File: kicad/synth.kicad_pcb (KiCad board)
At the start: 2 copper layers, 154.9 x 102.9 mm, 279 parts, among them CON101 SD_Card, CON201 K375A (DJK-02A), J301 KATE_3.5MM_6, J302 KATE_3.5MM_6, J401 KATE_3.5MM_6, J402 KATE_3.5MM_6, J403 KATE_3.5MM_6, P101 CONN_01X05, P102 CONN_01X03, P103 CONN_01X03, P104 47346-0001, P105 CONN_01X01, P106 DIN_5, P301 CONN_02X04, P302 CONN_01X03, Q101 MMBTA42, Q201 FDS6675, Q202 IRF7313PBF, Q301 Si2301DS, Q302 BC817, Q401 Si2301DS, Q402 Si2301DS, Q403 Si2301DS, SW101 SW_PUSH, SW102 SW_PUSH, T201 TRANS_CUSTOM, U101 STM32F405R, U102 USBLC6-2, U103 AD1955, U104 HCPL0453, U201 LM78L12ACZ, U202 79L12, U203 MC33269-SO8, U204 TPS76333DBV, U205 LP2985LV, U206 LP2985LV, U301 OP275S, U302 OP275S, U303 LM4864, U304 LM4864, U305 OP275S, U401 AD824, Y101 25MHz

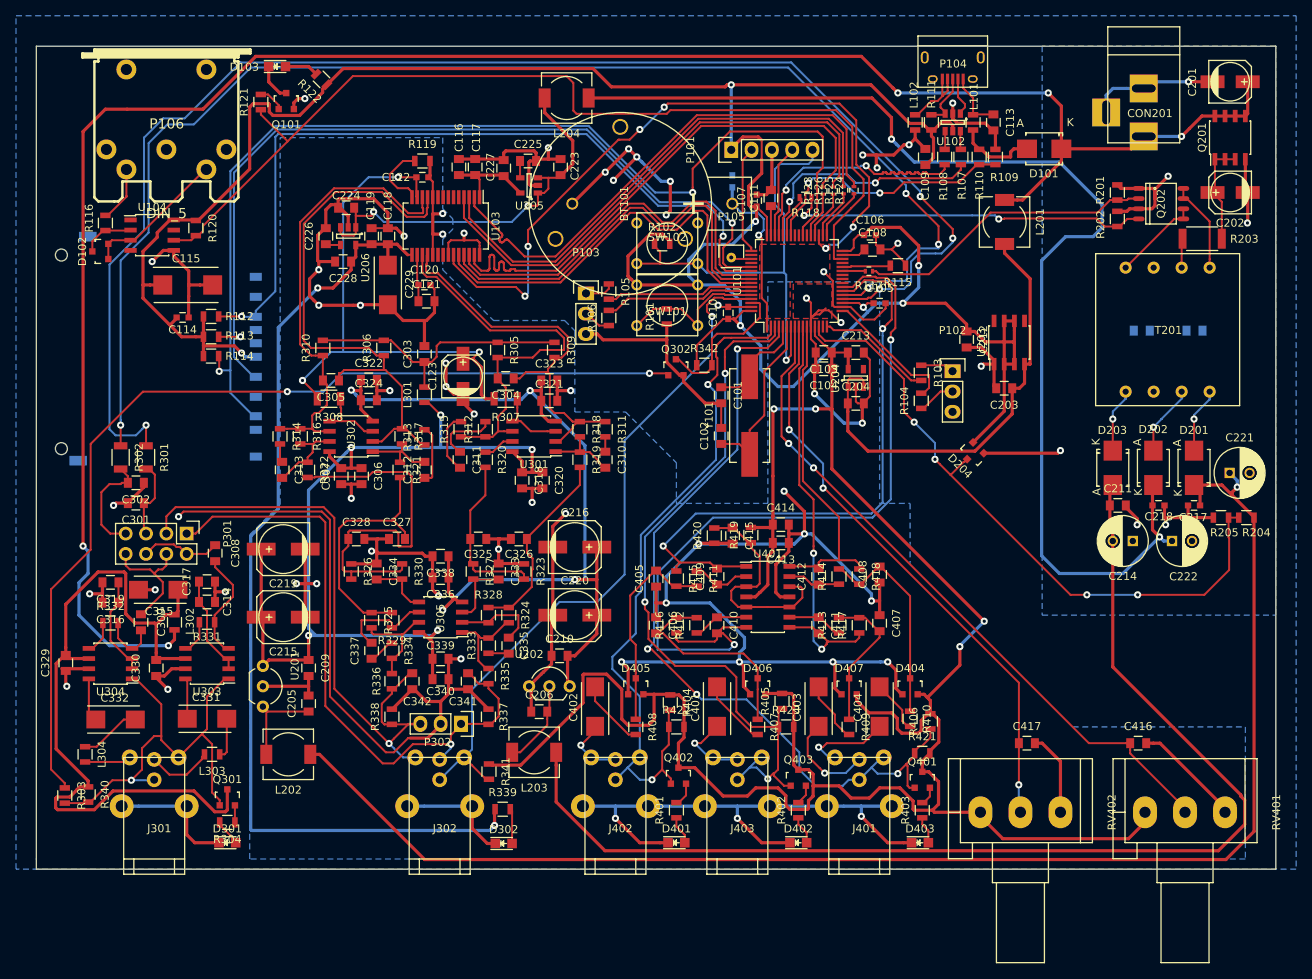
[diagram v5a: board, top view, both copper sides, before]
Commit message: version sent to rezonit
modified usb connector pads to smd
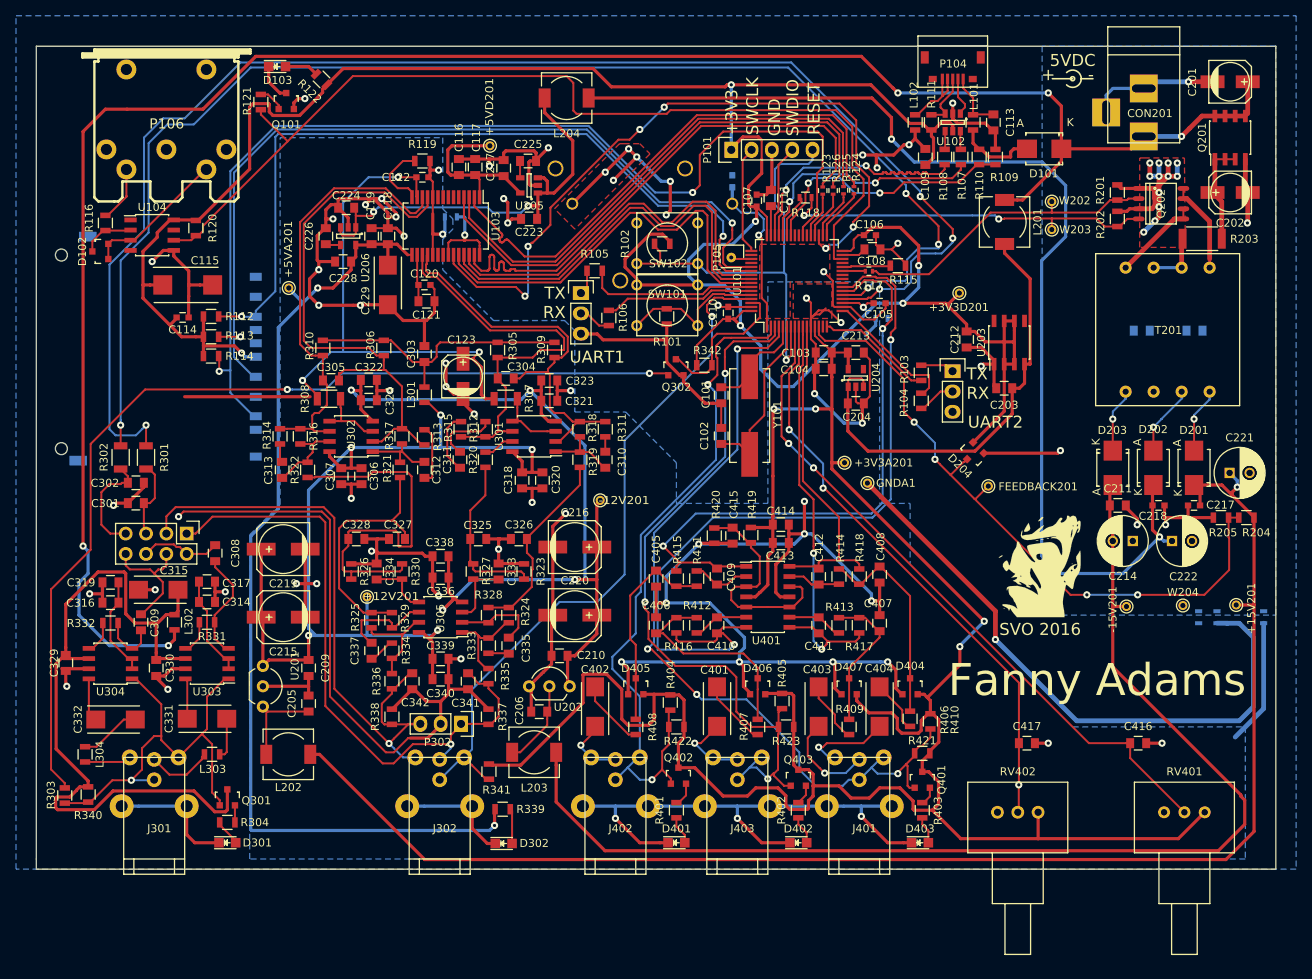
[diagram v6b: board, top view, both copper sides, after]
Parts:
- added +12V201: TST, Connect:PINTST, F.Cu at (54.0, 119.6)
- added +15V201: TST+15V, Connect:PINTST, F.Cu at (162.7, 120.7)
- added +3V3A201: TST, Connect:PINTST, F.Cu at (113.7, 102.9)
- added +3V3D201: TST, Connect:PINTST, F.Cu at (128.1, 81.7)
- added +5VA201: TST, Connect:PINTST, F.Cu at (44.3, 81.0)
- added +5VD201: TST, Connect:PINTST, F.Cu at (69.4, 63.2)
- added -12V201: TST, Connect:PINTST, F.Cu at (83.2, 107.6)
- added -15V201: TST-15V, Connect:PINTST, F.Cu at (149.0, 120.8)
- added FEEDBACK201: TST, Connect:PINTST, F.Cu at (131.7, 105.8)
- added G***: LOGO, svo_xface:svo-xface, F.Cu at (136.9, 115.8)
- added GNDA1: TST, Connect:PINTST, F.Cu at (116.6, 105.4)
- added JP101: Jumper_NC_Small, Resistors_SMD:R_0603, B.Cu at (64.5, 72.1)
- added JP102: Jumper_NC_Small, Resistors_SMD:R_0603, B.Cu at (118.4, 84.8)
- added JP103: Jumper_NC_Small, Resistors_SMD:R_0603, B.Cu at (158.0, 122.2)
- added JP104: Jumper_NC_Small, Resistors_SMD:R_0603, B.Cu at (138.2, 121.2)
- added JP105: Jumper_NC_Small, Resistors_SMD:R_0603, B.Cu at (166.1, 122.2)
- added JP106: Jumper_NC_Small, Resistors_SMD:R_0603, B.Cu at (160.3, 122.2)
- added W202: TST, Connect:PINTST, F.Cu at (139.6, 70.2)
- added W203: TST, Connect:PINTST, F.Cu at (139.6, 73.7)
- added W204: TST, Connect:PINTST, F.Cu at (156.0, 120.7)
- BT101: moved to B.Cu
- RV401, RV402: footprint Potentiometers:Potentiometer_Alps-RK16-single_largePads -> Potentiometers:Potentiometer_Spectrol-Type148-Type149_Single
- moved RV402 7.87 mm to (132.8, 146.6), turned to 0 degrees
- moved RV401 7.62 mm to (153.7, 146.6), turned to 0 degrees
- moved C223 7.58 mm to (74.3, 72.4), turned to 180 degrees
- moved R105 3.15 mm to (82.5, 78.9), turned to 0 degrees
- moved P103 0.64 mm to (80.8, 81.7)
- turned BT101 to 270 degrees
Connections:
- T201 pad 3: Net-(T201-Pad3) -> Net-(R203-Pad1)
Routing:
- net GNDA: track 542.7 -> 624.2 mm, vias 37 -> 44
- net GNDPWR: track 62.5 -> 84.1 mm, vias 6 -> 17
- net (no net): track 0.00 -> 15.7 mm
- net +3V3A_CPU: track 268.9 -> 280.2 mm
- net +5VD_DAC: track 12.3 -> 22.1 mm
- net GNDD: track 207.2 -> 214.7 mm, vias 24 -> 27
- net /megapower/+7V5: track 146.7 -> 139.7 mm
- net -12VOPA: track 116.8 -> 122.8 mm
- net +12VOPA: track 120.6 -> 125.4 mm
- net Net-(R203-Pad1): track 3.67 -> 7.17 mm
- net /UART1_TX: track 18.4 -> 21.5 mm
- net Net-(C223-Pad1): track 50.3 -> 53.0 mm
- net +5VA_DAC: track 122.7 -> 125.3 mm
- net +3V3D_CPU: track 337.8 -> 340.3 mm
- net /megapower/VFEEDBACK: track 81.4 -> 83.8 mm
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- added copper zone on F.Cu, net GNDPWR
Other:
- board text added: "+"
- board text added: "+3V3"
- board text added: "-"
- board text added: "5VDC"
- board text added: "Fanny Adams"
- board text added: "GND"
- board text added: "RESET"
- board text added: "SVO 2016"
- board text added: "SWCLK"
- board text added: "SWDIO"
- board text added: "TX RX"
- board text added: "UART1"
- board text added: "UART2"

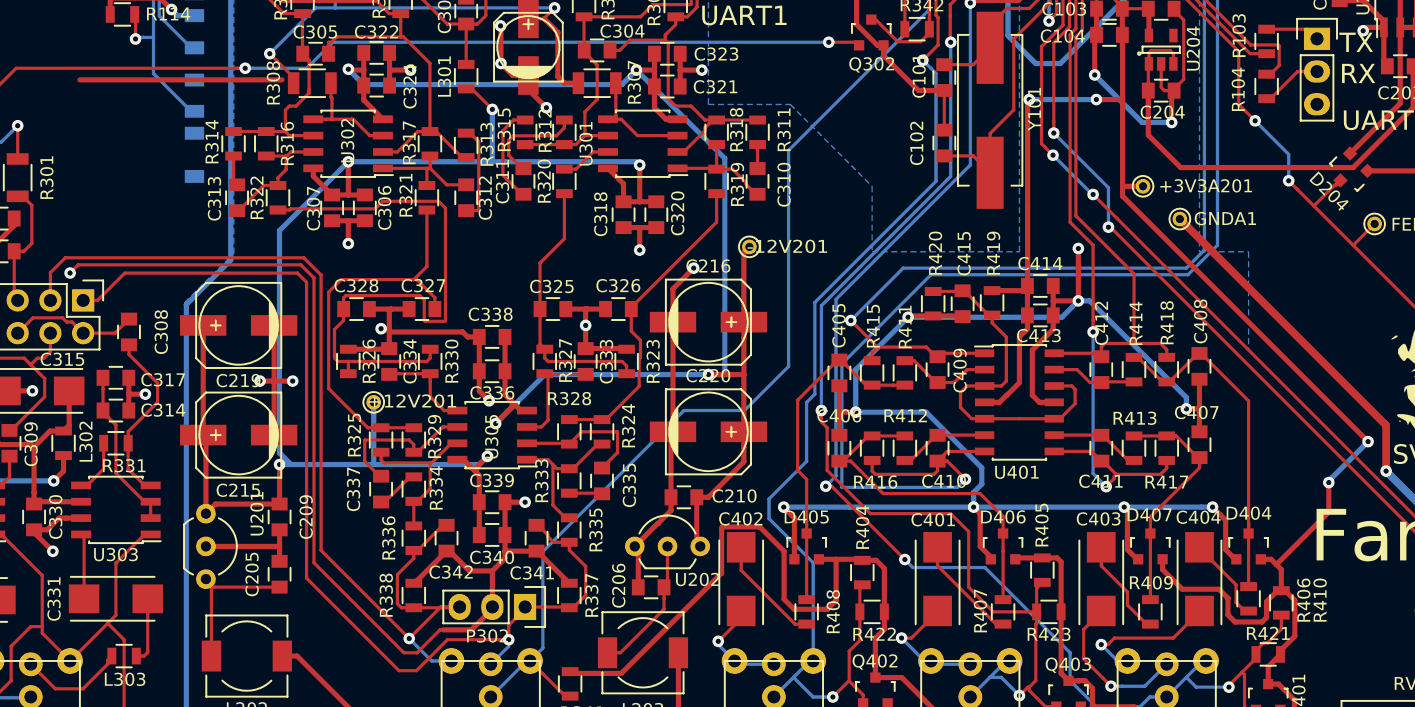
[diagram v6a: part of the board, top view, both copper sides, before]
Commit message: fixed p-mosfets
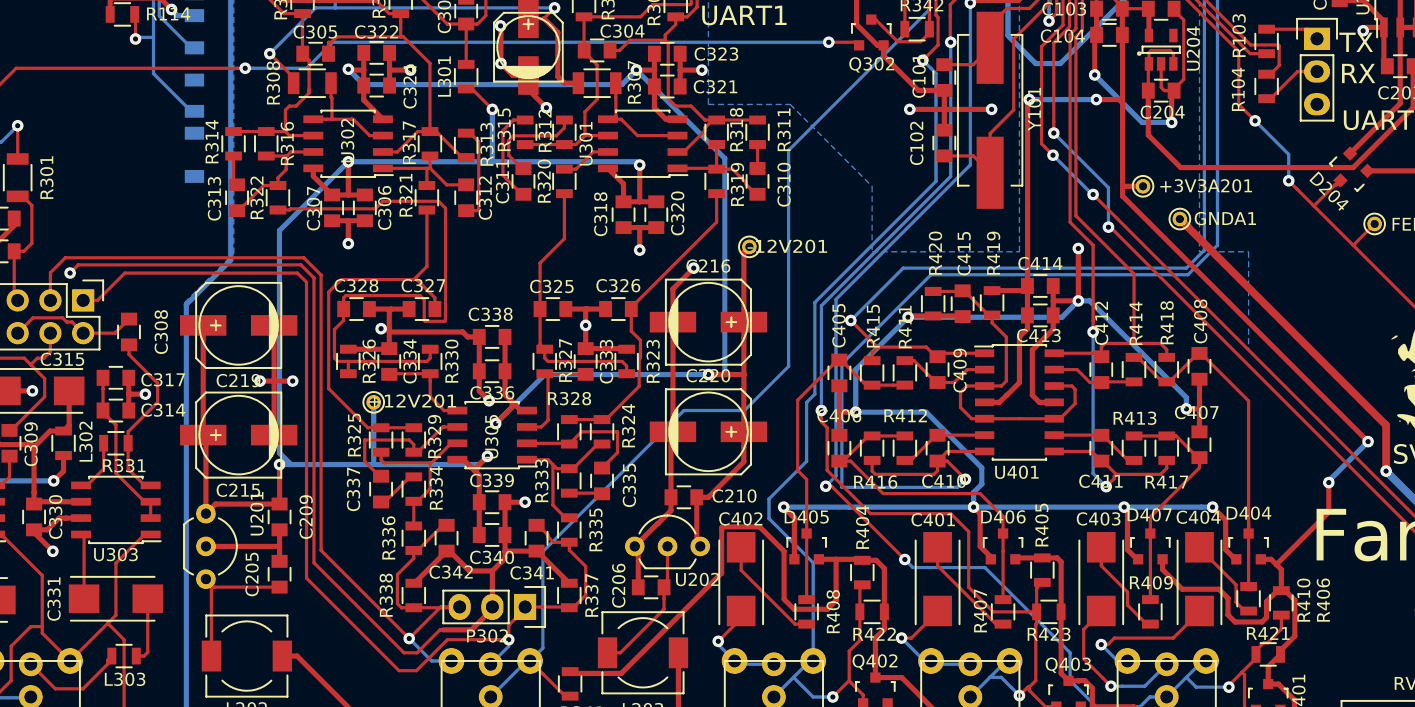
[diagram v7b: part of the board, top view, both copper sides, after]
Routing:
- net (no net): track 15.7 -> 0.00 mm
- net GNDD: track 214.7 -> 221.1 mm, vias 27 -> 29
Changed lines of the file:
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@@
   (general
     (links 615)
-    (no_connects 1)
-    (area 12.624999 50.724999 167.715001 153.745001)
+    (no_connects 0)
+    (area -1.143001 35.25 183.974286 167.853)
     (thickness 1.6)
     (drawings 26)
-    (tracks 3053)
+    (tracks 3057)
     (zones 0)
     (modules 299)
@@
   (page A4)
   (layers
-    (0 F.Cu signal hide)
-    (31 B.Cu signal hide)
-    (32 B.Adhes user hide)
-    (33 F.Adhes user hide)
-    (34 B.Paste user hide)
-    (35 F.Paste user hide)
+    (0 F.Cu signal)
+    (31 B.Cu signal)
+    (32 B.Adhes user)
+    (33 F.Adhes user)
+    (34 B.Paste user)
+    (35 F.Paste user)
     (36 B.SilkS user)
-    (37 F.SilkS user hide)
+    (37 F.SilkS user)
     (38 B.Mask user)
     (39 F.Mask user)
@@
   )
   (setup
-    (last_trace_width 0.4)
+    (last_trace_width 0.25)
     (user_trace_width 0.2)
     (user_trace_width 0.25)
@@
     (pad_to_mask_clearance 0.2)
     (aux_axis_origin 0 0)
-    (visible_elements 7FFC0801)
+    (visible_elements 7FFEFFFF)
     (pcbplotparams
       (layerselection 0x010e0_80000001)
@@
     (tags "resistor 0805")
     (attr smd)
-    (fp_text reference R406 (at 0.193 1.778 90) (layer F.SilkS)
+    (fp_text reference R406 (at 0.193 3.302 90) (layer F.SilkS)
       (effects (font (size 1 1) (thickness 0.15)))
     )
@@
     (tags "resistor 0805")
     (attr smd)
-    (fp_text reference R410 (at 0.127 -5.588 270) (layer F.SilkS)
+    (fp_text reference R410 (at 0.127 -4.318 270) (layer F.SilkS)
       (effects (font (size 1 1) (thickness 0.15)))
     )
@@
   (gr_line (start 167.64 50.8) (end 12.7 50.8) (layer Edge.Cuts) (width 0.15))
   (gr_line (start 12.7 50.8) (end 12.7 152.4) (layer Edge.Cuts) (width 0.15))
-  (segment (start 31.242 94.615) (end 46.921999 94.615) (width 0.4) (layer F.Cu) (net 0))
   (segment (start 99.695 68.441) (end 99.695 70.485) (width 0.4) (layer B.Cu) (net 1))
   (segment (start 102.87 71.628) (end 100.838 71.628) (width 0.25) (layer B.Cu) (net 1))
@@
   (segment (start 104.022487 82.940487) (end 103.378 82.296) (width 0.25) (layer F.Cu) (net 1))
   (segment (start 104.022487 85.844911) (end 104.022487 82.940487) (width 0.25) (layer F.Cu) (net 1))
+  (via (at 95.631 96.901) (size 0.9) (drill 0.4) (layers F.Cu B.Cu) (net 2))
+  (segment (start 98.310987 96.901) (end 95.631 96.901) (width 0.4) (layer F.Cu) (net 2))
+  (segment (start 98.310987 96.901) (end 98.310987 98.512411) (width 0.4) (layer F.Cu) (net 2))
+  (segment (start 98.310987 95.432411) (end 98.310987 96.901) (width 0.4) (layer F.Cu) (net 2))
+  (segment (start 98.310987 96.901) (end 101.981 96.901) (width 0.4) (layer F.Cu) (net 2))
+  (via (at 101.981 96.901) (size 0.9) (drill 0.4) (layers F.Cu B.Cu) (net 2))
   (segment (start 66.167 72.136) (end 66.256401 72.225401) (width 0.4) (layer B.Cu) (net 2))
   (segment (start 66.256401 72.225401) (end 66.256401 74.41002) (width 0.4) (layer B.Cu) (net 2))
@@
   (segment (start 132.588 63.693) (end 132.588 61.579) (width 0.4) (layer F.Cu) (net 2))
   (segment (start 132.588 61.579) (end 132.334 61.325) (width 0.4) (layer F.Cu) (net 2))
-  (segment (start 98.310987 95.432411) (end 98.310987 98.512411) (width 0.25) (layer F.Cu) (net 2))
   (segment (start 117.6535 74.422) (end 117.6535 75.6325) (width 0.25) (layer F.Cu) (net 2))
   (segment (start 117.6535 75.6325) (end 118.221 76.2) (width 0.25) (layer F.Cu) (net 2))

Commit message: circuit fixes
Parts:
- added R343, R344: 20K, Resistors_SMD:R_0805, F.Cu at (90.2, 163.7)
- C315: value 22.0 -> 220.0/6V
- C416, C417: value 1.0 -> 0.1
- Q302: value BC817 -> IRLML2502
- R112, R114: value 47K -> 10K
- R113: value 47K -> N/C
- R339: value 10K -> 330
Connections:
- Q301 pad 2: Net-(Q301-Pad2) -> /audioout/+5VHEAD
- Q301 pad 3: /audioout/+5VHEAD -> Net-(Q301-Pad3)
- Q401 pad 2: Net-(Q401-Pad2) -> +3V3A_CPU
- Q401 pad 3: +3V3A_CPU -> Net-(Q401-Pad3)
- Q402 pad 2: Net-(Q402-Pad2) -> +3V3A_CPU
- Q402 pad 3: +3V3A_CPU -> Net-(Q402-Pad3)
- Q403 pad 2: Net-(Q403-Pad2) -> +3V3A_CPU
- Q403 pad 3: +3V3A_CPU -> Net-(Q403-Pad3)
- R304 pad 1: Net-(Q301-Pad2) -> Net-(Q301-Pad3)
- R320 pad 1: Net-(R320-Pad1) -> Net-(C311-Pad2)
- R331 pad 2: Net-(C308-Pad1) -> Net-(R331-Pad2)
- R332 pad 2: Net-(C309-Pad1) -> Net-(R332-Pad2)
- R401 pad 2: Net-(Q402-Pad2) -> Net-(Q402-Pad3)
- R402 pad 2: Net-(Q403-Pad2) -> Net-(Q403-Pad3)
- R403 pad 2: Net-(Q401-Pad2) -> Net-(Q401-Pad3)
- U301 pad 7: Net-(R320-Pad1) -> Net-(C311-Pad2)
- U303 pad 4: Net-(C308-Pad1) -> Net-(R331-Pad2)
- U304 pad 4: Net-(C309-Pad1) -> Net-(R332-Pad2)
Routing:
- net +3V3A_CPU: track 280.2 -> 245.9 mm
- net Net-(Q402-Pad3): track 0.00 -> 22.3 mm
- net Net-(Q301-Pad3): track 0.00 -> 20.2 mm
- net /audioout/+5VHEAD: track 93.3 -> 75.2 mm
- net Net-(Q403-Pad3): track 0.00 -> 16.5 mm
- net Net-(R331-Pad2): track 0.00 -> 13.0 mm
- net Net-(C308-Pad1): track 13.8 -> 0.75 mm
- net Net-(C311-Pad2): track 7.73 -> 15.6 mm
- net Net-(R332-Pad2): track 0.00 -> 6.43 mm
- net Net-(C309-Pad1): track 7.18 -> 0.75 mm
- net Net-(R320-Pad1): track 3.93 -> 0.00 mm
- net Net-(Q401-Pad3): track 0.00 -> 3.42 mm
- net Net-(Q402-Pad2): track 3.04 -> 0.00 mm
- net Net-(Q403-Pad2): track 2.51 -> 0.00 mm
- net Net-(Q401-Pad2): track 2.36 -> 0.00 mm
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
